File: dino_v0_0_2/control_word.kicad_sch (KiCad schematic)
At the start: 8 parts, among them U28 74LS138, U29 74LS138, U30 74LS138, U62 74LS02

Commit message: Machine Complete
All ten DINO modules bench-proven on the ATmega2560 rig: root, pc,
microcode, control_word, mdr, registers, mar, memory, alu, io. Coverage
lint reports 0 gaps and 0 pending.

Test modules (mod_*.c) plus host-tested expect models (cw/mdr/reg/mar/
mem/alu_expect.h) — pure logic, no AVR headers, exhaustive host tests
written RED before any bench run. Every assertion was netlist-verified
against the schematic before it was encoded.

Generators, so no table is hand-maintained:
  kicad_contracts.py   contracts + pinmap from the KiCad netlist
  microcode_gen.py     microcode ROM images
  progrom_gen.py       program ROM (DIAG + the milestone program)
  layout_gen.py        breadboard placement, slot maps, wiring guides

Two house rules learned the hard way and now codified in BRINGUP.md:
  mirror-witness   a write-then-read through one bus bank is
                   permutation-blind; every module needs an asymmetric
                   path (this is what caught the flipped PORTF->MDR bank)
  phantom power    rig lines feed DUT VCC through input clamp diodes, so
                   an unpowered board reads fine; every module gets a
                   power test holding outputs at the non-sourcing level

The ALU slot map in layout_gen.py is AS-BUILT and FROZEN — read off the
strip by beeping each slot to its chip pin, not derived. Once a strip is
populated its slot map is copper.

Housekeeping: .gitignore for __pycache__, KiCad .lck, Obsidian workspace
state, and compiled host-test binaries; those are untracked here.

Next: the integration ladder (INT-A/B/B2/C/D/E), then free-run of
LDAI 5; LDBI 3; ADD; OUT; HALT — the milestone, where the machine adds
two numbers.

Co-Authored-By: Claude Opus 5 (1M context) <noreply@anthropic.com>
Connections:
- net SRC_ACTIVE: now reaches U28.15 (O0)
- no-connect marks 6 -> 5
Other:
- note added: "MODULE CONTRACT — generated, do not hand-edit (kicad_contracts.py --stamp) IN: FLAG_Z <- ALU Module IN: CW0-8 <- Microcode_Decoder OUT: ~{ALU_OUT} -> ALU Module, Memory Data Register OUT: ~{REG_A_LOAD}, ~{REG_B_LOAD} -> ALU Module, Register Modules OUT: ~{MAR_HI_LOAD}, ~{MAR_LO_LOAD} -> Memory Address Regiser OUT: SRC_ACTIVE, ~{IR_LOAD}, ~{MDR_OUT}, ~{RAM_LOAD} -> Memory Data Register OUT: ~{SW_O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"
- note removed: "MODULE CONTRACT — generated, do not hand-edit (kicad_contracts.py --stamp) IN: FLAG_Z <- ALU Module IN: CW0-8 <- Microcode_Decoder OUT: ~{ALU_OUT} -> ALU Module OUT: ~{REG_A_LOAD}, ~{REG_B_LOAD} -> ALU Module, Register Modules OUT: ~{MAR_HI_LOAD}, ~{MAR_LO_LOAD} -> Memory Address Regiser OUT: ~{IR_LOAD}, ~{MDR_OUT}, ~{RAM_LOAD} -> Memory Data Register OUT: ~{RAM_OUT}, ~{ROM_OUT} -> Memory, Memory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"
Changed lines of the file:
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@@
+		)
+	)
+	(text "MODULE CONTRACT — generated, do not hand-edit (kicad_contracts.py --stamp)\nIN: FLAG_Z <- ALU Module\nIN: CW0-8 <- Microcode_Decoder\nOUT: ~{ALU_OUT} -> ALU Module, Memory Data Register\nOUT: ~{REG_A_LOAD}, ~{REG_B_LOAD} -> ALU Module, Register Modules\nOUT: ~{MAR_HI_LOAD}, ~{MAR_LO_LOAD} -> Memory Address Regiser\nOUT: SRC_ACTIVE, ~{IR_LOAD}, ~{MDR_OUT}, ~{RAM_LOAD} -> Memory Data Register\nOUT: ~{SW_OUT} -> Memory Data Register, Output\nOUT: ~{RAM_OUT}, ~{ROM_OUT} -> Memory, Memory Data Register\nOUT: ~{PC_CLEAR}, ~{PC_LOAD} -> Program Counter\nOUT: ~{REG_A_OUT}, ~{REG_B_OUT}, ~{REG_C_LOAD}, ~{REG_C_OUT}, ~{REG_OUT_LOAD} -> Register Modules"
+		(exclude_from_sim no)
+		(at 159.766 170.434 0)
+		(effects
+			(font
+				(size 1.27 1.27)
+			)
+			(justify left bottom)
 		)
 	)
@@
 		)
 	)
-	(text "MODULE CONTRACT — generated, do not hand-edit (kicad_contracts.py --stamp)\nIN: FLAG_Z <- ALU Module\nIN: CW0-8 <- Microcode_Decoder\nOUT: ~{ALU_OUT} -> ALU Module\nOUT: ~{REG_A_LOAD}, ~{REG_B_LOAD} -> ALU Module, Register Modules\nOUT: ~{MAR_HI_LOAD}, ~{MAR_LO_LOAD} -> Memory Address Regiser\nOUT: ~{IR_LOAD}, ~{MDR_OUT}, ~{RAM_LOAD} -> Memory Data Register\nOUT: ~{RAM_OUT}, ~{ROM_OUT} -> Memory, Memory Data Register\nOUT: ~{SW_OUT} -> Output\nOUT: ~{PC_CLEAR}, ~{PC_LOAD} -> Program Counter\nOUT: ~{REG_A_OUT}, ~{REG_B_OUT}, ~{REG_C_LOAD}, ~{REG_C_OUT}, ~{REG_OUT_LOAD} -> Register Modules"
-		(exclude_from_sim no)
-		(at 159.766 170.434 0)
-		(effects
-			(font
-				(size 1.27 1.27)
-			)
-			(justify left bottom)
-		)
-	)
 	(text "[11:9] ALU Bus\n"
 		(exclude_from_sim no)
@@
 	)
 	(no_connect
-		(at 104.14 88.9)
-	)
-	(no_connect
 		(at 176.53 67.31)
 	)
@@
 	(wire
 		(pts
+			(xy 104.14 88.9) (xy 99.06 88.9)
+		)
+		(stroke
+			(width 0)
+			(type default)
+		)
+	)
+	(wire
+		(pts
 			(xy 180.34 57.15) (xy 176.53 57.15)
 		)
@@
 		)
 	)
+	(label "SRC_ACTIVE"
+		(at 99.06 88.9 180)
+		(effects
+			(font
+				(size 1.27 1.27)
+			)
+			(justify right bottom)
+		)
+	)

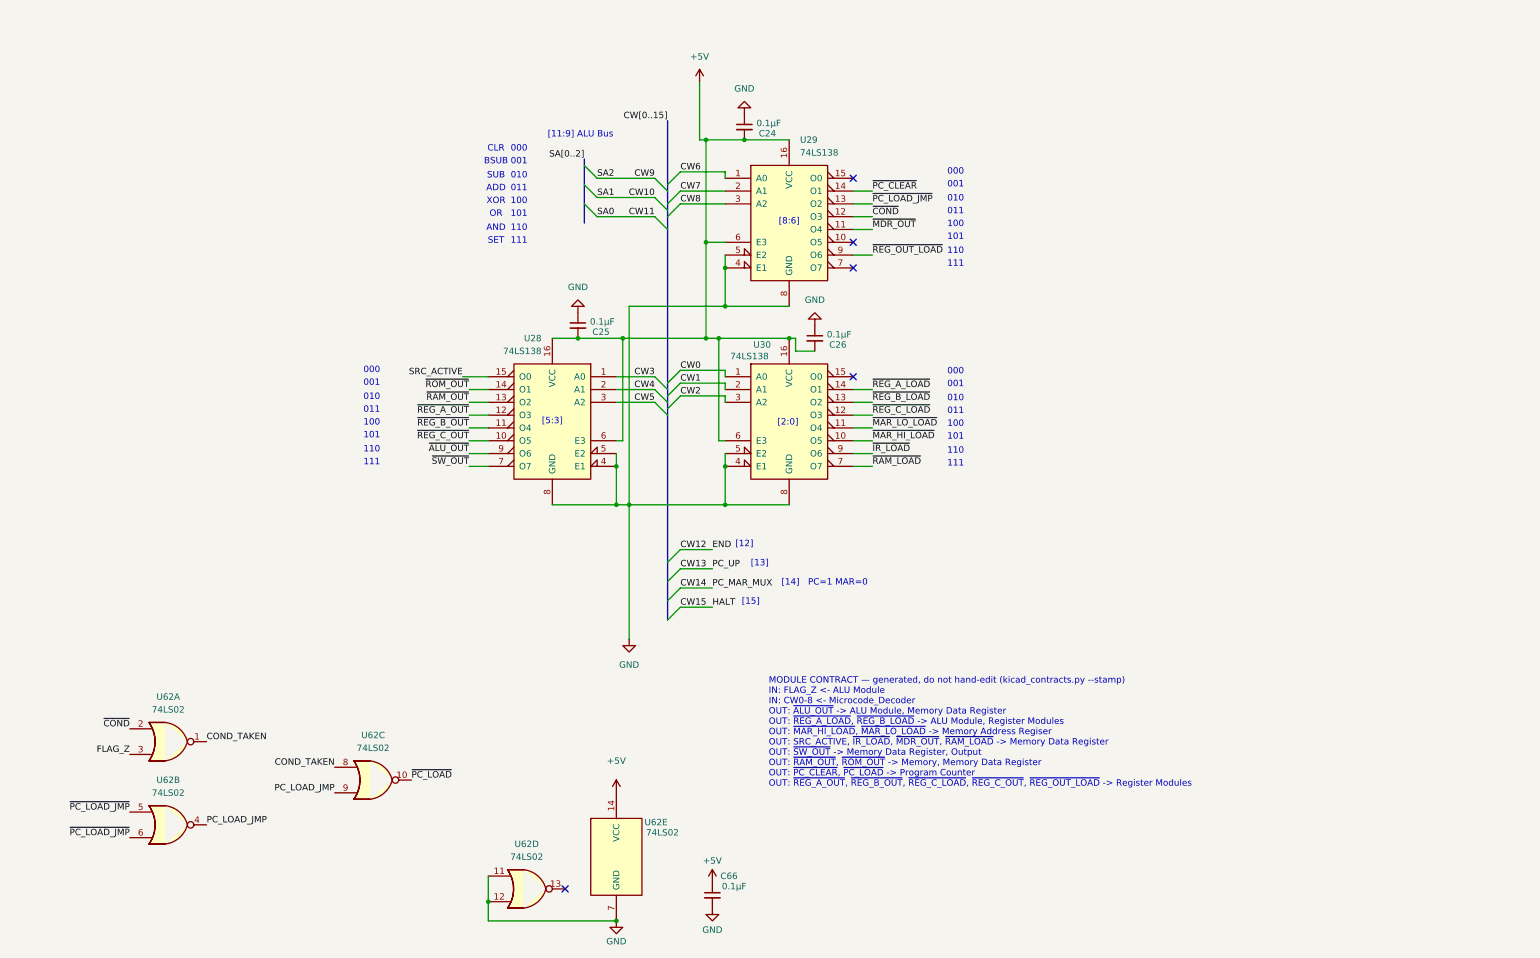
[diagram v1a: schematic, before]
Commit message: Stack pointer + third microcode EEPROM: schematic, tooling, and ISA
Twelve chips, four sheets, seven instructions. The whole stack executes on
the gate model; the rig is detached so nothing has run on real hardware.

  U23         AT28C64B   third microcode EEPROM, CW16-23     microcode
  U70 / U71   '138       SRC / DST bank-1 decoders           control_word
  U63-U66     '169       16-bit stack pointer                stack_pointer
  U67 / U68   '245       SP hi/lo readback -> MDR            stack_pointer
  U69         '08        ~{SP_CE} = AND(~SP_UP, ~SP_DOWN)    stack_pointer
  U72 / U73   '245       PC0-7 / PC8-15 -> MDR               mdr

  LXISP 0x14   CALL 0x33   RET 0x34
  PUSHA 0x61   POPA 0x62   PUSHB 0x63   POPB 0x64

THE CONTROL WORD IS 24 BITS. Every new bit is polarised so 0xFF -- an erased
AT28C64B -- is today's machine, the same reasoning that made HALT=0xFF. Only
~{SRC_BANK} and ~{DST_BANK} are wired; ~{CIN_SEL}, ~{MISC_BANK},
~{ADDR_SEL1}, FLAG_SEL0/1 and FLAG_POL are burned into all 4096 rows and
wired to nothing, so no reburn is needed when their decode arrives.

Bank switching costs zero inverters: E3 is active-high and E1 active-low, so
bank 0 hangs off E3 and bank 1 off E1 of the same bit. SRC/DST codes 8-15 are
bank 1; word() derives the bank bit FROM the code, so a caller cannot select
SP_LO and forget to switch banks.

MISC IS NOW FULL. U29's O5/O7 were the last two free codes and the stack
spends both. O0 is the NONE slot and can never be reclaimed.

Deviations from dino_hardware_growth_plan.md, corrected inline there:

  - SRC3/DST3/MISC3 -> ~{SRC_BANK}/~{DST_BANK}/~{MISC_BANK}. A '138 has three
    address pins; the new bit is an ENABLE, not a fourth.
  - COND[2:0] -> FLAG_SEL0/FLAG_SEL1/FLAG_POL. COND0 loses KiCad's alias sort
    to CW21, steals the net off the CW bus, and produces net_not_bus_member.
  - CIN is a SELECT, not a carry value: one ROM bit cannot BE the carry.
  - MISC had two free codes, not three, and SP_LOAD is a DST d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
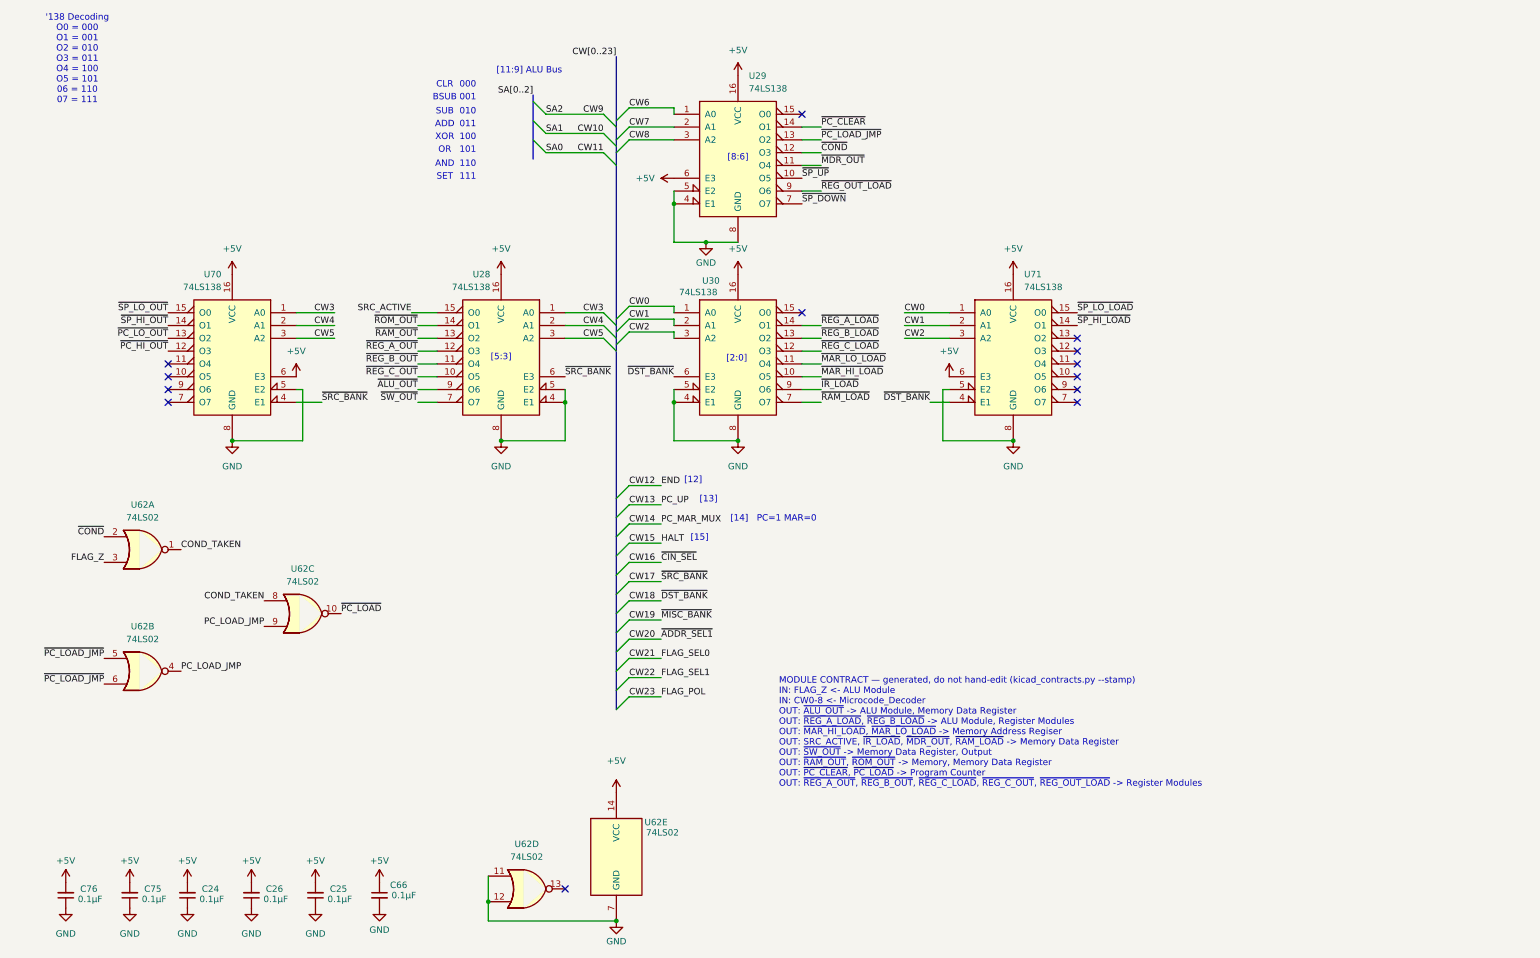
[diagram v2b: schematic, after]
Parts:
- added C75, C76: 0.1µF, symbol Device:C_Small
- added U70, U71: 74LS138, symbol 74xx:74LS138
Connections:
- net +5V: now also C75.2, C76.2, U70.16 (VCC), U70.6 (E3), U71.16 (VCC), U71.6 (E3); no longer U28.6 (E3), U30.6 (E3)
- net CW0: now also U71.1 (A0)
- net CW1: now also U71.2 (A1)
- net CW2: now also U71.3 (A2)
- net CW3: now also U70.1 (A0)
- net CW4: now also U70.2 (A1)
- net CW5: now also U70.3 (A2)
- net GND: now also C75.1, C76.1, U70.5 (E2), U70.8 (GND), U71.5 (E2), U71.8 (GND)
- net ~{SP_UP}: now reaches U29.10 (O5)
- net ~{SP_DOWN}: now reaches U29.7 (O7)
- new net CW17: U28.6 (E3), U70.4 (E1)
- new net CW18: U30.6 (E3), U71.4 (E1)
- new net ~{PC_HI_OUT}: U70.12 (O3)
- new net ~{PC_LO_OUT}: U70.13 (O2)
- new net ~{SP_HI_LOAD}: U71.14 (O1)
- new net ~{SP_HI_OUT}: U70.14 (O1)
- new net ~{SP_LO_LOAD}: U71.15 (O0)
- new net ~{SP_LO_OUT}: U70.15 (O0)
- no-connect marks 5 -> 13
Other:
- note added: "'138 Decoding O0 = 000 O1 = 001 O2 = 010 O3 = 011 O4 = 100 O5 = 101 06 = 110 07 = 111"
- moved on the sheet: C24, C25, C26, C66, U28, U29, U30, U62A, U62B, U62C

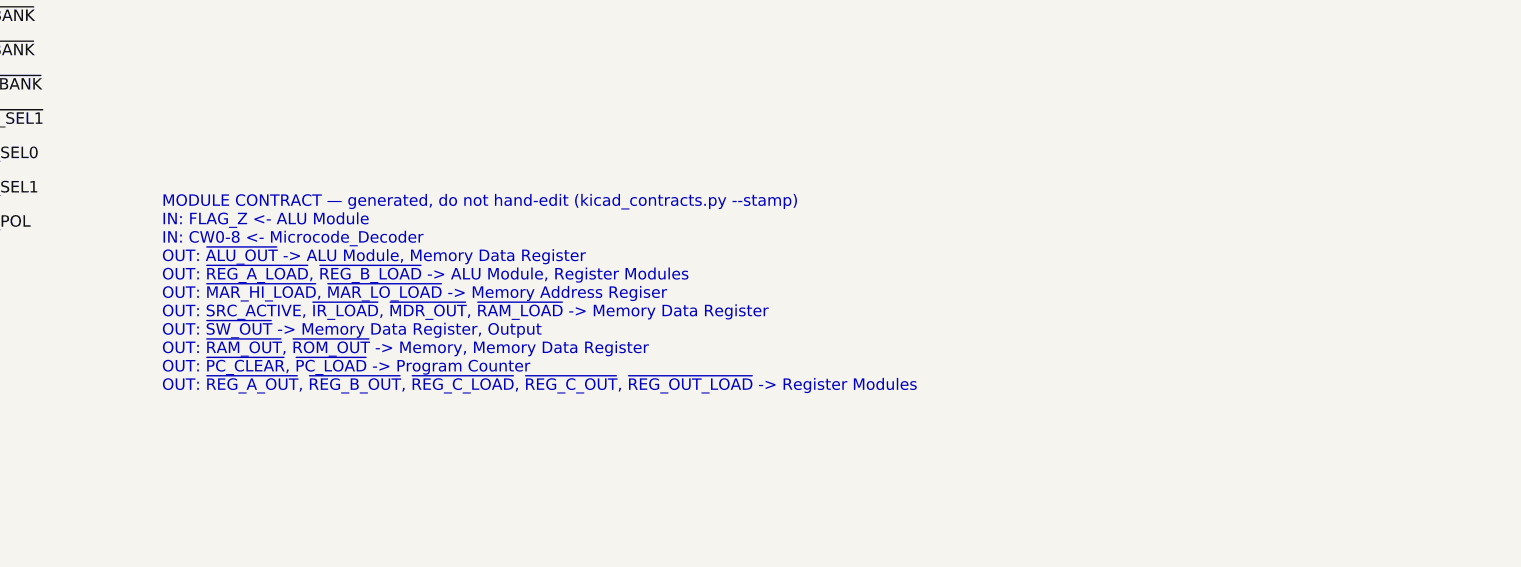
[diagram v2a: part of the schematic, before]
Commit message: feat: phase D on silicon — the machine executes from RAM
PROG_ramexec returns 0x6E. The PC has been above 0x7FFF and FETCH_RAM has
been high, both for the first time in this machine's life.

The missing condition was never "is this a fetch." ~ROM_OUT is asserted for
every src=ROM — opcode fetch, LDAI's immediate, LDA/STA/JMP/CALL operand
bytes — so an instruction living in RAM must read its operands from RAM
too. The condition is "a ROM-side read was requested, but the address is
above 0x7FFF":

    FETCH_RAM = NOR(~ROM_OUT, ~RAM_EN)

Six gate sections, no new IC. All six were free on U22/U37/U39, already in
sockets on the MDR board, where ~ROM_OUT and ~RAM_OUT already sit feeding
READS_IDLE. Only ~RAM_EN had to be brought in.

    U22 g3   FETCH_RAM     = NOR(~ROM_OUT, ~RAM_EN)
    U22 g4   ROM_BUF_ON    = NOR(~ROM_OUT, FETCH_RAM)
    U37 inv4 ~{FETCH_RAM}
    U37 inv6 ~{ROM_BUF_EN} = OR(~ROM_OUT, FETCH_RAM)   -> U19.19
    U37 inv5 ~{RAM_OE_G}   = AND(~RAM_OUT, ~FETCH_RAM) -> U26.22 + U51.9
    U39 g4   RAM_OE_ON     = NAND(~RAM_OUT, ~FETCH_RAM)

Two pin lifts on the memory board, eleven wires. U24.22 stays on ~ROM_OUT:
U24's own ~CE = M15 already deselects the ROM chip at RAM addresses.

Gating ~RAM_OUT upstream is what keeps this at six gates rather than eight.
U51 is a 7400 computing ~RAM_MDR_EN = AND(~RAM_OUT, ~WRITE_DIR), so one
gate on ~RAM_OUT moves both the RAM chip's ~OE and its buffer's ~CE.

Re-proved before building: all 15 src=ROM microcode rows carry mux_pc=True,
FETCH included, and FILL is src=NONE. A ROM-side read can now land in RAM,
so the standing "ROM reads are exempt from the src=RAM -> MAR loop" rule was
no longer free. It holds — MAR never drives M during a ROM-side read, and a
runaway opcode cannot open the loop either.

The witness is not permutation-blind. If the fetch had still come from ROM,
PC=0x9000 presents A0-A14 = 0x1000 to U24, which is 0xFF fill, which is
HALT, so the poison would have survived as 0xFF. 0x6E is 0x8B - 0x1D,
compu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
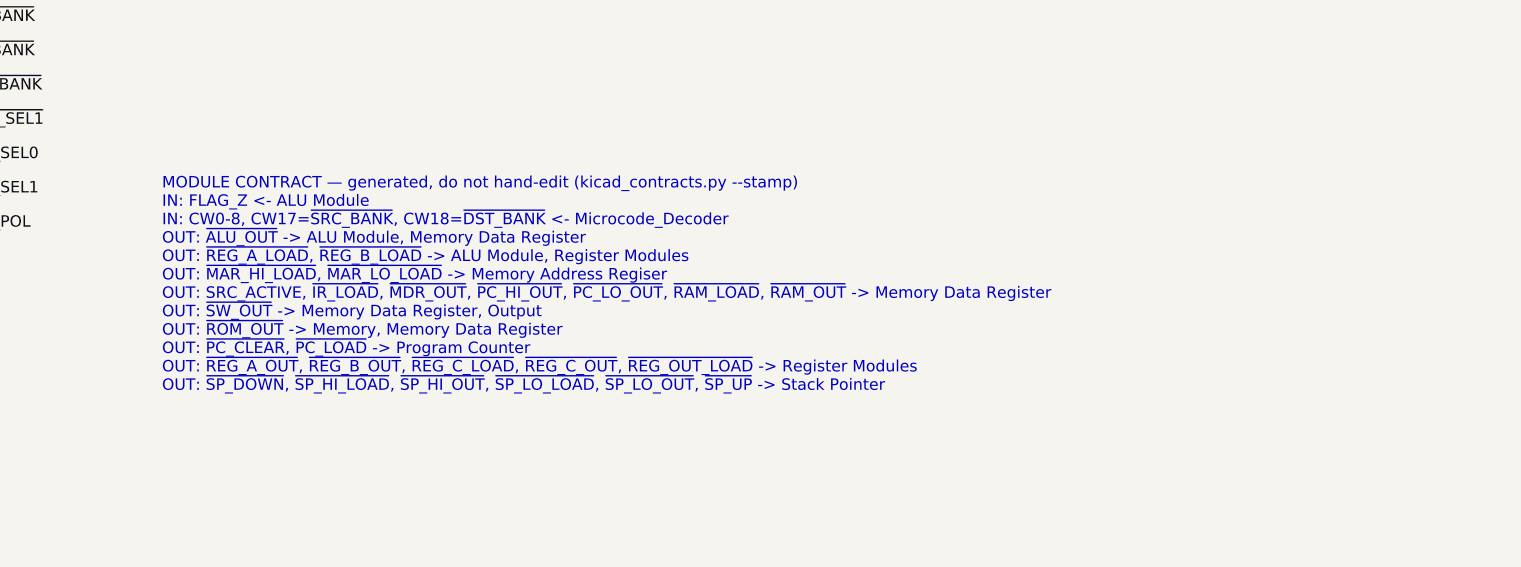
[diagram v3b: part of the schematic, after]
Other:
- note added: "MODULE CONTRACT — generated, do not hand-edit (kicad_contracts.py --stamp) IN: FLAG_Z <- ALU Module IN: CW0-8, CW17=~{SRC_BANK}, CW18=~{DST_BANK} <- Microcode_Decoder OUT: ~{ALU_OUT} -> ALU Module, Memory Data Register OUT: ~{REG_A_LOAD}, ~{REG_B_LOAD} -> ALU Module, Register Modules OUT: ~{MAR_HI_LOAD}, ~{MAR_LO_LOAD} -> Memory Address Regiser OUT: SRC_ACTIVE, ~{IR_LOAD}, ~{MDR_OUT}, ~{PC_HI_OUT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"
- note removed: "MODULE CONTRACT — generated, do not hand-edit (kicad_contracts.py --stamp) IN: FLAG_Z <- ALU Module IN: CW0-8 <- Microcode_Decoder OUT: ~{ALU_OUT} -> ALU Module, Memory Data Register OUT: ~{REG_A_LOAD}, ~{REG_B_LOAD} -> ALU Module, Register Modules OUT: ~{MAR_HI_LOAD}, ~{MAR_LO_LOAD} -> Memory Address Regiser OUT: SRC_ACTIVE, ~{IR_LOAD}, ~{MDR_OUT}, ~{RAM_LOAD} -> Memory Data Register OUT: ~{SW_O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"
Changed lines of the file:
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@@
 		)
 	)
-	(text "MODULE CONTRACT — generated, do not hand-edit (kicad_contracts.py --stamp)\nIN: FLAG_Z <- ALU Module\nIN: CW0-8 <- Microcode_Decoder\nOUT: ~{ALU_OUT} -> ALU Module, Memory Data Register\nOUT: ~{REG_A_LOAD}, ~{REG_B_LOAD} -> ALU Module, Register Modules\nOUT: ~{MAR_HI_LOAD}, ~{MAR_LO_LOAD} -> Memory Address Regiser\nOUT: SRC_ACTIVE, ~{IR_LOAD}, ~{MDR_OUT}, ~{RAM_LOAD} -> Memory Data Register\nOUT: ~{SW_OUT} -> Memory Data Register, Output\nOUT: ~{RAM_OUT}, ~{ROM_OUT} -> Memory, Memory Data Register\nOUT: ~{PC_CLEAR}, ~{PC_LOAD} -> Program Counter\nOUT: ~{REG_A_OUT}, ~{REG_B_OUT}, ~{REG_C_LOAD}, ~{REG_C_OUT}, ~{REG_OUT_LOAD} -> Register Modules"
-		(exclude_from_sim no)
-		(at 161.798 170.434 0)
-		(effects
-			(font
-				(size 1.27 1.27)
-			)
-			(justify left bottom)
-		)
-	)
 	(text "XOR"
 		(exclude_from_sim no)
@@
 		)
 	)
+	(text "MODULE CONTRACT — generated, do not hand-edit (kicad_contracts.py --stamp)\nIN: FLAG_Z <- ALU Module\nIN: CW0-8, CW17=~{SRC_BANK}, CW18=~{DST_BANK} <- Microcode_Decoder\nOUT: ~{ALU_OUT} -> ALU Module, Memory Data Register\nOUT: ~{REG_A_LOAD}, ~{REG_B_LOAD} -> ALU Module, Register Modules\nOUT: ~{MAR_HI_LOAD}, ~{MAR_LO_LOAD} -> Memory Address Regiser\nOUT: SRC_ACTIVE, ~{IR_LOAD}, ~{MDR_OUT}, ~{PC_HI_OUT}, ~{PC_LO_OUT}, ~{RAM_LOAD}, ~{RAM_OUT} -> Memory Data Register\nOUT: ~{SW_OUT} -> Memory Data Register, Output\nOUT: ~{ROM_OUT} -> Memory, Memory Data Register\nOUT: ~{PC_CLEAR}, ~{PC_LOAD} -> Program Counter\nOUT: ~{REG_A_OUT}, ~{REG_B_OUT}, ~{REG_C_LOAD}, ~{REG_C_OUT}, ~{REG_OUT_LOAD} -> Register Modules\nOUT: ~{SP_DOWN}, ~{SP_HI_LOAD}, ~{SP_HI_OUT}, ~{SP_LO_LOAD}, ~{SP_LO_OUT}, ~{SP_UP} -> Stack Pointer"
+		(exclude_from_sim no)
+		(at 161.798 170.434 0)
+		(effects
+			(font
+				(size 1.27 1.27)
+			)
+			(justify left bottom)
+		)
+	)
